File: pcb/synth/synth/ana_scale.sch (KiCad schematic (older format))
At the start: 11 parts, among them U14 OPA4172

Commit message: final pcb designs and initial i2c
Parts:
- R61: value 10k -> 91k
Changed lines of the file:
@@
 $Descr A4 11693 8268
 encoding utf-8
-Sheet 9 9
+Sheet 7 9
 Title ""
 Date ""
@@
 AR Path="/5DECCC25/5DC59994/5DC124B2" Ref="U15"  Part="1"
 AR Path="/5DECCC25/5DC59C98/5DC124B2" Ref="U16"  Part="1"
-F 0 "U16" H 4050 3767 50  0000 C CNN
+F 0 "U14" H 4050 3767 50  0000 C CNN
 F 1 "OPA4172" H 4050 3676 50  0000 C CNN
 F 2 "Package_SO:SOIC-14_3.9x8.7mm_P1.27mm" H 4000 3500 50  0001 C CNN
@@
 AR Path="/5DECCC25/5DC59994/5DC13438" Ref="U15"  Part="2"
 AR Path="/5DECCC25/5DC59C98/5DC13438" Ref="U16"  Part="2"
-F 0 "U16" H 4050 4817 50  0000 C CNN
+F 0 "U14" H 4050 4817 50  0000 C CNN
 F 1 "OPA4172" H 4050 4726 50  0000 C CNN
 F 2 "Package_SO:SOIC-14_3.9x8.7mm_P1.27mm" H 4000 4550 50  0001 C CNN
@@
 AR Path="/5DECCC25/5DC59994/5DC14C1E" Ref="U15"  Part="4"
 AR Path="/5DECCC25/5DC59C98/5DC14C1E" Ref="U16"  Part="4"
-F 0 "U16" H 6900 4367 50  0000 C CNN
+F 0 "U14" H 6900 4367 50  0000 C CNN
 F 1 "OPA4172" H 6900 4276 50  0000 C CNN
 F 2 "Package_SO:SOIC-14_3.9x8.7mm_P1.27mm" H 6850 4100 50  0001 C CNN
@@
 AR Path="/5DECCC25/5DC59994/5DC1560D" Ref="U15"  Part="5"
 AR Path="/5DECCC25/5DC59C98/5DC1560D" Ref="U16"  Part="5"
-F 0 "U16" H 5708 2546 50  0000 L CNN
+F 0 "U14" H 5708 2546 50  0000 L CNN
 F 1 "OPA4172" H 5708 2455 50  0000 L CNN
 F 2 "Package_SO:SOIC-14_3.9x8.7mm_P1.27mm" H 5700 2600 50  0001 C CNN
@@
 AR Path="/5DECCC25/5DC59994/5DC16F21" Ref="#PWR0191"  Part="1"
 AR Path="/5DECCC25/5DC59C98/5DC16F21" Ref="#PWR0198"  Part="1"
-F 0 "#PWR0198" H 5650 1950 50  0001 C CNN
+F 0 "#PWR0184" H 5650 1950 50  0001 C CNN
 F 1 "+12V" H 5665 2273 50  0000 C CNN
 F 2 "" H 5650 2100 50  0001 C CNN
@@
 AR Path="/5DECCC25/5DC59994/5DC1793A" Ref="#PWR0192"  Part="1"
 AR Path="/5DECCC25/5DC59C98/5DC1793A" Ref="#PWR0199"  Part="1"
-F 0 "#PWR0199" H 5650 3000 50  0001 C CNN
+F 0 "#PWR0185" H 5650 3000 50  0001 C CNN
 F 1 "-12V" H 5665 3073 50  0000 C CNN
 F 2 "" H 5650 2900 50  0001 C CNN
@@
 AR Path="/5DECCC25/5DC59994/5DC18ECD" Ref="C41"  Part="1"
 AR Path="/5DECCC25/5DC59C98/5DC18ECD" Ref="C43"  Part="1"
-F 0 "C43" H 5265 2346 50  0000 L CNN
+F 0 "C39" H 5265 2346 50  0000 L CNN
 F 1 "0.1u" H 5265 2255 50  0000 L CNN
 F 2 "Capacitor_SMD:C_0603_1608Metric_Pad1.05x0.95mm_HandSolder" H 5188 2150 50  0001 C CNN
@@
 AR Path="/5DECCC25/5DC59994/5DC19710" Ref="C42"  Part="1"
 AR Path="/5DECCC25/5DC59C98/5DC19710" Ref="C44"  Part="1"
-F 0 "C44" H 5265 2746 50  0000 L CNN
+F 0 "C40" H 5265 2746 50  0000 L CNN
 F 1 "0.1u" H 5265 2655 50  0000 L CNN
 F 2 "Capacitor_SMD:C_0603_1608Metric_Pad1.05x0.95mm_HandSolder" H 5188 2550 50  0001 C CNN
@@
 AR Path="/5DECCC25/5DC59994/5DC1F094" Ref="#PWR0193"  Part="1"
 AR Path="/5DECCC25/5DC59C98/5DC1F094" Ref="#PWR0200"  Part="1"
-F 0 "#PWR0200" H 4900 2300 50  0001 C CNN
+F 0 "#PWR0186" H 4900 2300 50  0001 C CNN
 F 1 "GND" H 4905 2377 50  0000 C CNN
 F 2 "" H 4900 2550 50  0001 C CNN
@@
 AR Path="/5DECCC25/5DC59994/5DC25E99" Ref="R64"  Part="1"
 AR Path="/5DECCC25/5DC59C98/5DC25E99" Ref="R72"  Part="1"
-F 0 "R72" H 3368 4196 50  0000 L CNN
+F 0 "R56" H 3368 4196 50  0000 L CNN
 F 1 "10k" H 3368 4105 50  0000 L CNN
 F 2 "Resistor_SMD:R_0603_1608Metric_Pad1.05x0.95mm_HandSolder" V 3340 4140 50  0001 C CNN
@@
 AR Path="/5DECCC25/5DC59994/5DC2680B" Ref="R66"  Part="1"
 AR Path="/5DECCC25/5DC59C98/5DC2680B" Ref="R74"  Part="1"
-F 0 "R74" H 3368 4596 50  0000 L CNN
+F 0 "R58" H 3368 4596 50  0000 L CNN
 F 1 "1.2k" H 3368 4505 50  0000 L CNN
 F 2 "Resistor_SMD:R_0603_1608Metric_Pad1.05x0.95mm_HandSolder" V 3340 4540 50  0001 C CNN
@@
 AR Path="/5DECCC25/5DC59994/5DC26D18" Ref="#PWR0194"  Part="1"
 AR Path="/5DECCC25/5DC59C98/5DC26D18" Ref="#PWR0201"  Part="1"
-F 0 "#PWR0201" H 3300 4500 50  0001 C CNN
+F 0 "#PWR0187" H 3300 4500 50  0001 C CNN
 F 1 "GND" H 3305 4577 50  0000 C CNN
 F 2 "" H 3300 4750 50  0001 C CNN
@@
 AR Path="/5DECCC25/5DC59994/5DC27DBE" Ref="#PWR0195"  Part="1"
 AR Path="/5DECCC25/5DC59C98/5DC27DBE" Ref="#PWR0202"  Part="1"
-F 0 "#PWR0202" H 3300 3800 50  0001 C CNN
+F 0 "#PWR0188" H 3300 3800 50  0001 C CNN
 F 1 "+12V" H 3315 4123 50  0000 C CNN
 F 2 "" H 3300 3950 50  0001 C CNN
@@
 AR Path="/5DECCC25/5DC59994/5DC2B548" Ref="R62"  Part="1"
 AR Path="/5DECCC25/5DC59C98/5DC2B548" Ref="R70"  Part="1"
-F 0 "R70" V 4805 4000 50  0000 C CNN
+F 0 "R54" V 4805 4000 50  0000 C CNN
 F 1 "10k" V 4714 4000 50  0000 C CNN
 F 2 "Resistor_SMD:R_0603_1608Metric_Pad1.05x0.95mm_HandSolder" V 4640 3990 50  0001 C CNN
@@
 AR Path="/5DECCC25/5DC59994/5DC2BE14" Ref="R65"  Part="1"
 AR Path="/5DECCC25/5DC59C98/5DC2BE14" Ref="R73"  Part="1"
-F 0 "R73" V 4487 4200 50  0000 C CNN
+F 0 "R57" V 4487 4200 50  0000 C CNN
 F 1 "10k" V 4396 4200 50  0000 C CNN
 F 2 "Resistor_SMD:R_0603_1608Metric_Pad1.05x0.95mm_HandSolder" V 4640 4190 50  0001 C CNN
@@
 AR Path="/5DECCC25/5DC59994/5DC30E8A" Ref="R67"  Part="1"
 AR Path="/5DECCC25/5DC59C98/5DC30E8A" Ref="R75"  Part="1"
-F 0 "R75" H 4832 4596 50  0000 R CNN
+F 0 "R59" H 4832 4596 50  0000 R CNN
 F 1 "10k" H 4832 4505 50  0000 R CNN
 F 2 "Resistor_SMD:R_0603_1608Metric_Pad1.05x0.95mm_HandSolder" V 4940 4540 50  0001 C CNN
@@
 AR Path="/5DECCC25/5DC59994/5DC32987" Ref="#PWR0196"  Part="1"
 AR Path="/5DECCC25/5DC59C98/5DC32987" Ref="#PWR0203"  Part="1"
-F 0 "#PWR0203" H 4900 4500 50  0001 C CNN
+F 0 "#PWR0189" H 4900 4500 50  0001 C CNN
 F 1 "GND" H 4905 4577 50  0000 C CNN
 F 2 "" H 4900 4750 50  0001 C CNN
@@
 AR Path="/5DECCC25/5DC59994/5DC343A6" Ref="R68"  Part="1"
 AR Path="/5DECCC25/5DC59C98/5DC343A6" Ref="R76"  Part="1"
-F 0 "R76" V 5605 4600 50  0000 C CNN
+F 0 "R60" V 5605 4600 50  0000 C CNN
 F 1 "10k" V 5514 4600 50  0000 C CNN
 F 2 "Resistor_SMD:R_0603_1608Metric_Pad1.05x0.95mm_HandSolder" V 5440 4590 50  0001 C CNN
@@
 AR Path="/5DECCC25/5DC59994/5DC385AE" Ref="R63"  Part="1"
 AR Path="/5DECCC25/5DC59C98/5DC385AE" Ref="R71"  Part="1"
-F 0 "R71" V 6255 4100 50  0000 C CNN
+F 0 "R55" V 6255 4100 50  0000 C CNN
 F 1 "10k" V 6164 4100 50  0000 C CNN
 F 2 "Resistor_SMD:R_0603_1608Metric_Pad1.05x0.95mm_HandSolder" V 6090 4090 50  0001 C CNN
@@
 AR Path="/5DECCC25/5DC59994/5DC14152" Ref="U15"  Part="3"
 AR Path="/5DECCC25/5DC59C98/5DC14152" Ref="U16"  Part="3"
-F 0 "U16" H 5400 4467 50  0000 C CNN
+F 0 "U14" H 5400 4467 50  0000 C CNN
 F 1 "OPA4172" H 5400 4376 50  0000 C CNN
 F 2 "Package_SO:SOIC-14_3.9x8.7mm_P1.27mm" H 5350 4200 50  0001 C CNN
@@
 AR Path="/5DECCC25/5DC59994/5DC42617" Ref="R69"  Part="1"
 AR Path="/5DECCC25/5DC59C98/5DC42617" Ref="R77"  Part="1"
-F 0 "R77" V 7105 4600 50  0000 C CNN
-F 1 "10k" V 7014 4600 50  0000 C CNN
+F 0 "R61" V 7105 4600 50  0000 C CNN
+F 1 "91k" V 7014 4600 50  0000 C CNN
 F 2 "Resistor_SMD:R_0603_1608Metric_Pad1.05x0.95mm_HandSolder" V 6940 4590 50  0001 C CNN
 F 3 "~" H 6900 4600 50  0001 C CNN
@@
 AR Path="/5DECCC25/5DC59994/5DC477F2" Ref="#PWR0197"  Part="1"
 AR Path="/5DECCC25/5DC59C98/5DC477F2" Ref="#PWR0204"  Part="1"
-F 0 "#PWR0204" H 6300 4500 50  0001 C CNN
+F 0 "#PWR0190" H 6300 4500 50  0001 C CNN
 F 1 "GND" H 6305 4577 50  0000 C CNN
 F 2 "" H 6300 4750 50  0001 C CNN

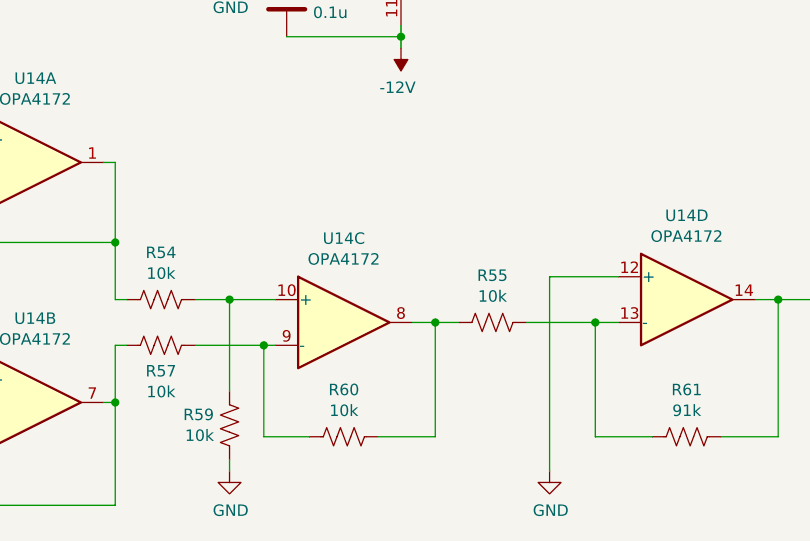
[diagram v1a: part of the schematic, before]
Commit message: implemented 2 wiproc design with one streaming to other and printing to terminal
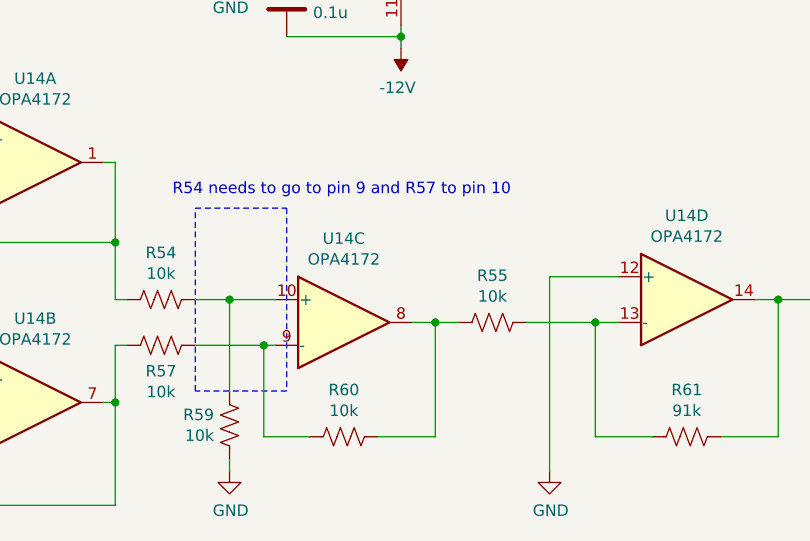
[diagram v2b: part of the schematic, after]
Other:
- note added: "R54 needs to go to pin 9 and R57 to pin 10"
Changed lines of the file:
@@
 Text HLabel 8150 4000 2    50   Output ~ 0
 AN_SCALED_OUT
+Wire Notes Line
+	5150 3600 5150 4400
+Wire Notes Line
+	5150 4400 4750 4400
+Wire Notes Line
+	4750 4400 4750 3600
+Wire Notes Line
+	4750 3600 5150 3600
+Text Notes 4650 3550 0    50   ~ 0
+R54 needs to go to pin 9 and R57 to pin 10
 $EndSCHEMATC
